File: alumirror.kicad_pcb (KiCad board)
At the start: 2 copper layers, 142.9 x 87.2 mm, 71 parts, among them J1 USB_C_Receptacle_USB2.0_16P_2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, J2 USB_C_Receptacle_USB2.0_16P_2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, K00 PG1350, K01 PG1350, K02 PG1350, K03 PG1350, K04 PG1350, K05 PG1350, K10 PG1350, K11 PG1350, K12 PG1350, K13 PG1350, K14 PG1350, K15 PG1350, K20 PG1350, K21 PG1350, K22 PG1350, K23 PG1350, K24 PG1350, K25 PG1350_1½U, K30 PG1350_1½U, K31 PG1350/SKQUCAA010, SW1 BOOT, U1 CH552T, U2 CH552T, U3 USBLC6-2P6, U4 USBLC6-2P6

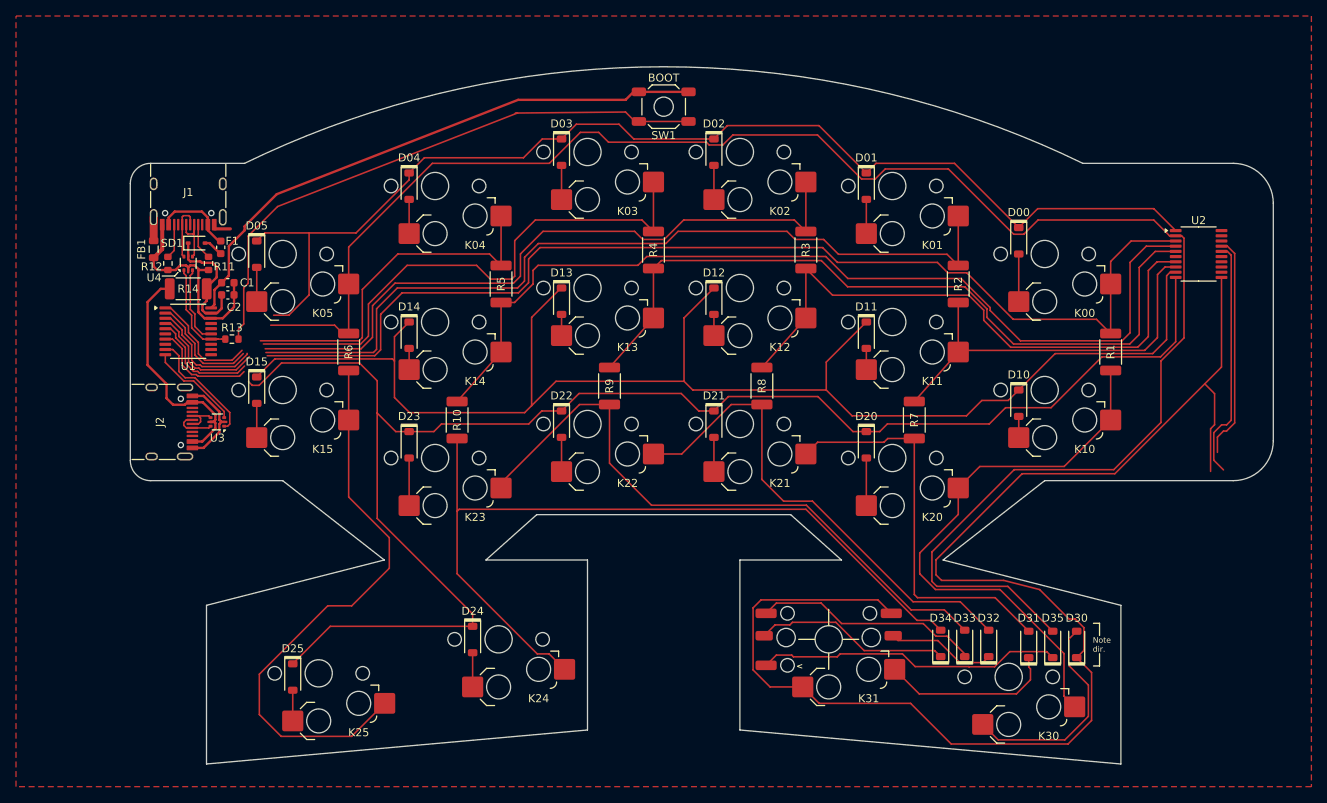
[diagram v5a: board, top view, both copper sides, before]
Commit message: Add LEDs
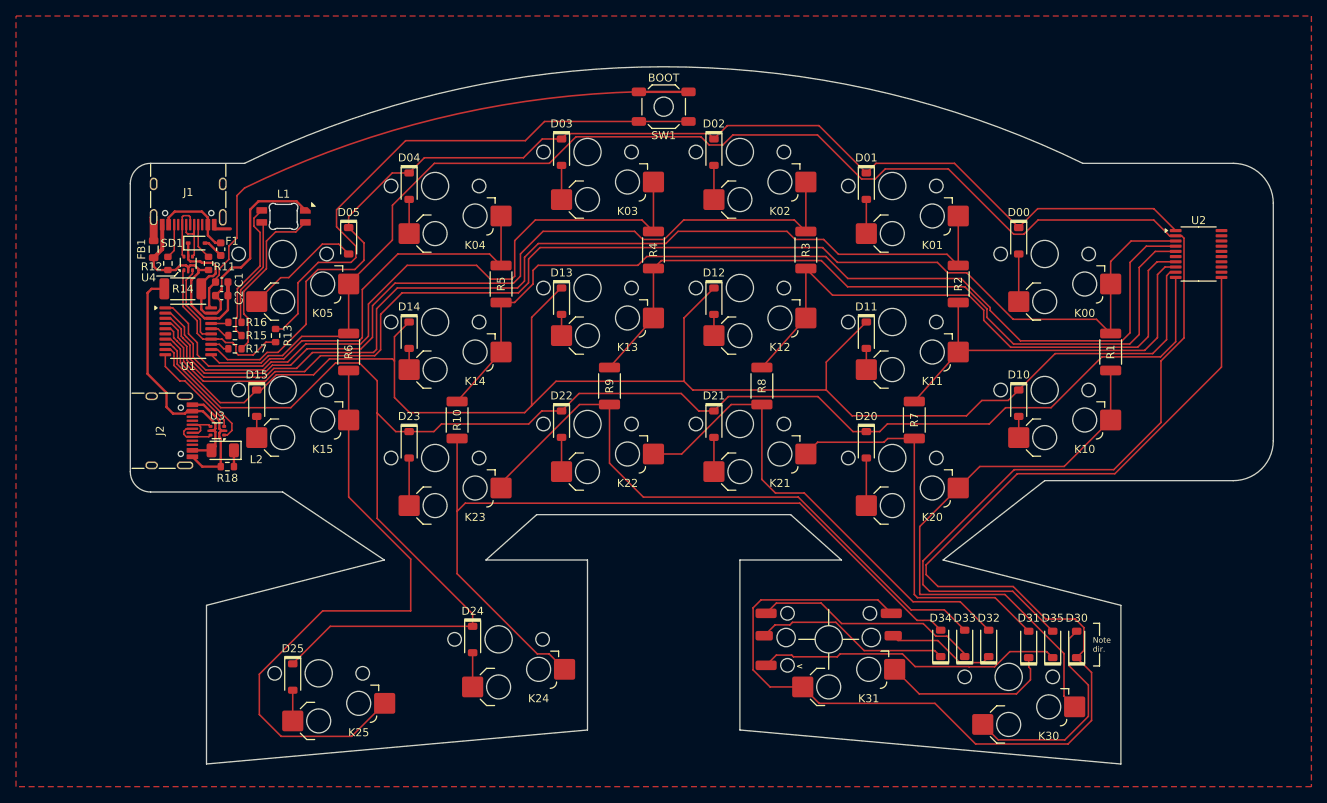
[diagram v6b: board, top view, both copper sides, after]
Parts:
- added L1: LED_6028R, PCM_marbastlib-various:LED_6028R, F.Cu at (104.9, 47.7)
- added L2: LED, LED_SMD:LED_1206_3216Metric, F.Cu at (97.3, 77.0)
- added R15: R, Resistor_SMD:R_0603_1608Metric, F.Cu at (98.8, 62.6)
- added R16: R, Resistor_SMD:R_0603_1608Metric, F.Cu at (98.8, 61.0)
- added R17: R, Resistor_SMD:R_0603_1608Metric, F.Cu at (98.8, 64.3)
- added R18: R, Resistor_SMD:R_0603_1608Metric, F.Cu at (97.9, 79.0)
- moved D05 11.6 mm to (113.0, 50.8)
- moved R13 5.48 mm to (103.9, 62.6), turned to 90 degrees
- moved D15 1.63 mm to (101.5, 71.1)
- moved J2 1.11 mm to (89.4, 74.5)
- moved U3 1.11 mm to (96.6, 74.5)
- moved C1 0.77 mm to (97.2, 55.9)
- moved C2 0.77 mm to (97.2, 57.6)
- moved R14 0.67 mm to (92.3, 56.8)
- moved F1 0.23 mm to (97.0, 51.8)
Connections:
- net +3V3_L renamed +3V3
- net BOOT_L renamed Net-(NT1-Pad1)
- net Net-(R13-Pad2) renamed /BOOT
- U1 pad 1: Col3L -> Col4L
- U1 pad 11: Col4L -> Col5
- U1 pad 12: Col5 -> Row0
- U1 pad 13: Row0 -> LED_B
- U1 pad 16: LED_B -> LED_R
- U1 pad 2: Col2L -> Col3L
- U1 pad 3: Col1L -> Col2L
- U1 pad 4: Col0 -> Col1L
- U1 pad 5: Row1 -> Col0
- U1 pad 7: Row2 -> Row1
- U1 pad 8: LED_R -> Row2
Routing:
- net +3V3: track 71.7 -> 23.1 mm
- net TX_R: track 30.0 -> 0.00 mm
- net RX_R: track 28.0 -> 0.00 mm
- net VCC_L: track 16.7 -> 38.2 mm
- net Net-(L1-BK): track 0.00 -> 21.0 mm
- net Col4L: track 44.9 -> 63.4 mm
- net Net-(L1-RK): track 0.00 -> 17.9 mm
- net Net-(L1-GK): track 0.00 -> 13.8 mm
- net Net-(D05-A): track 4.28 -> 15.0 mm
- net Col5: track 221.1 -> 231.0 mm
- net Row3R: track 177.6 -> 168.3 mm
- net Net-(NT1-Pad1): track 0.00 -> 8.67 mm
- net /Col5': track 72.1 -> 79.0 mm
- net Row0: track 144.5 -> 151.2 mm
- net Col3L: track 82.5 -> 86.5 mm
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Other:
- outline, holes or cut-outs redrawn

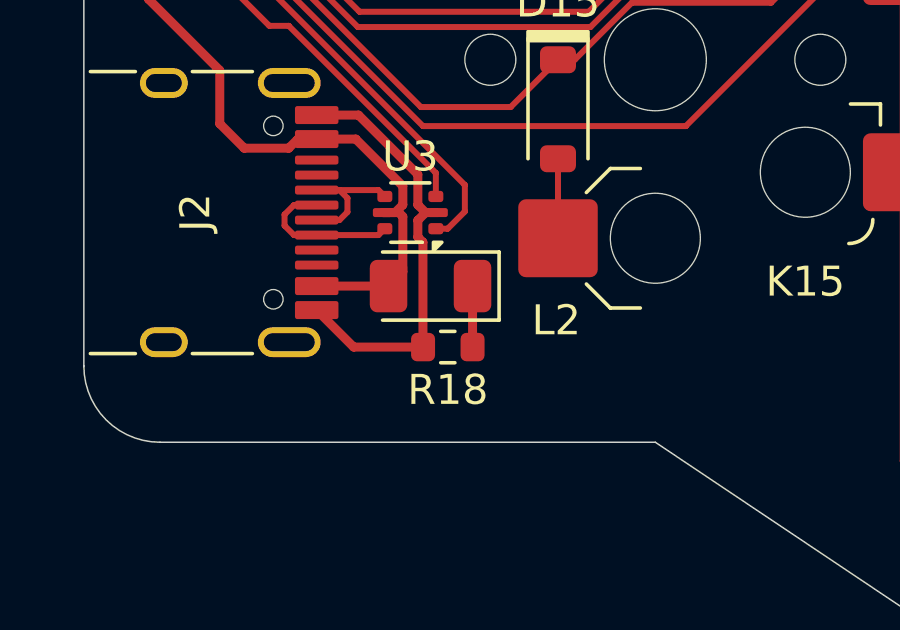
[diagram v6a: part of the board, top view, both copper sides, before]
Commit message: Use smaller (0603) power LED
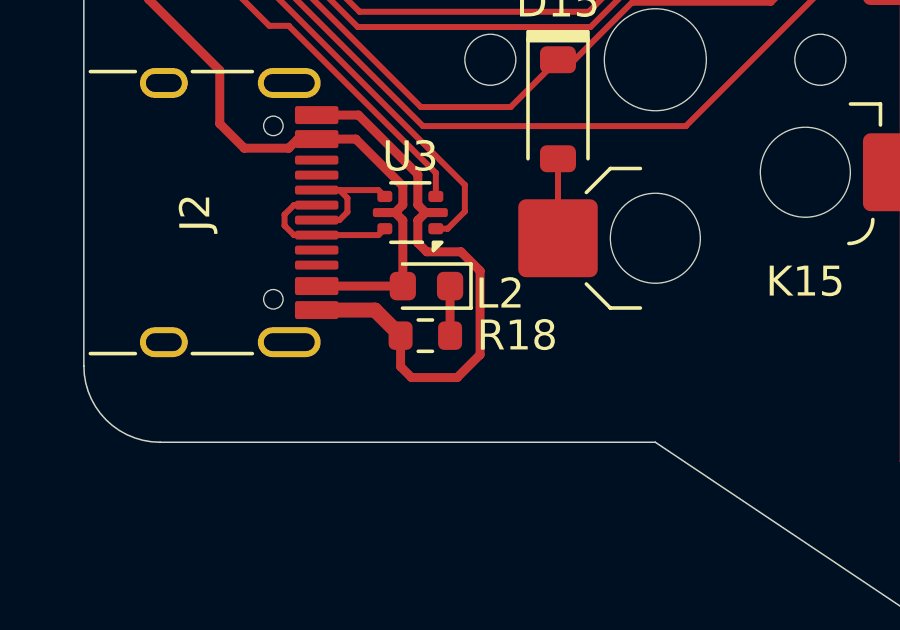
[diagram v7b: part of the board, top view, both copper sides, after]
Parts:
- L2: footprint LED_SMD:LED_1206_3216Metric -> LED_SMD:LED_0603_1608Metric
- moved R18 0.84 mm to (97.1, 78.6)
- moved L2 0.14 mm to (97.1, 77.0)
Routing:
- net GND: track 44.5 -> 49.4 mm
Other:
- board text added: "Top edge arc centre point"

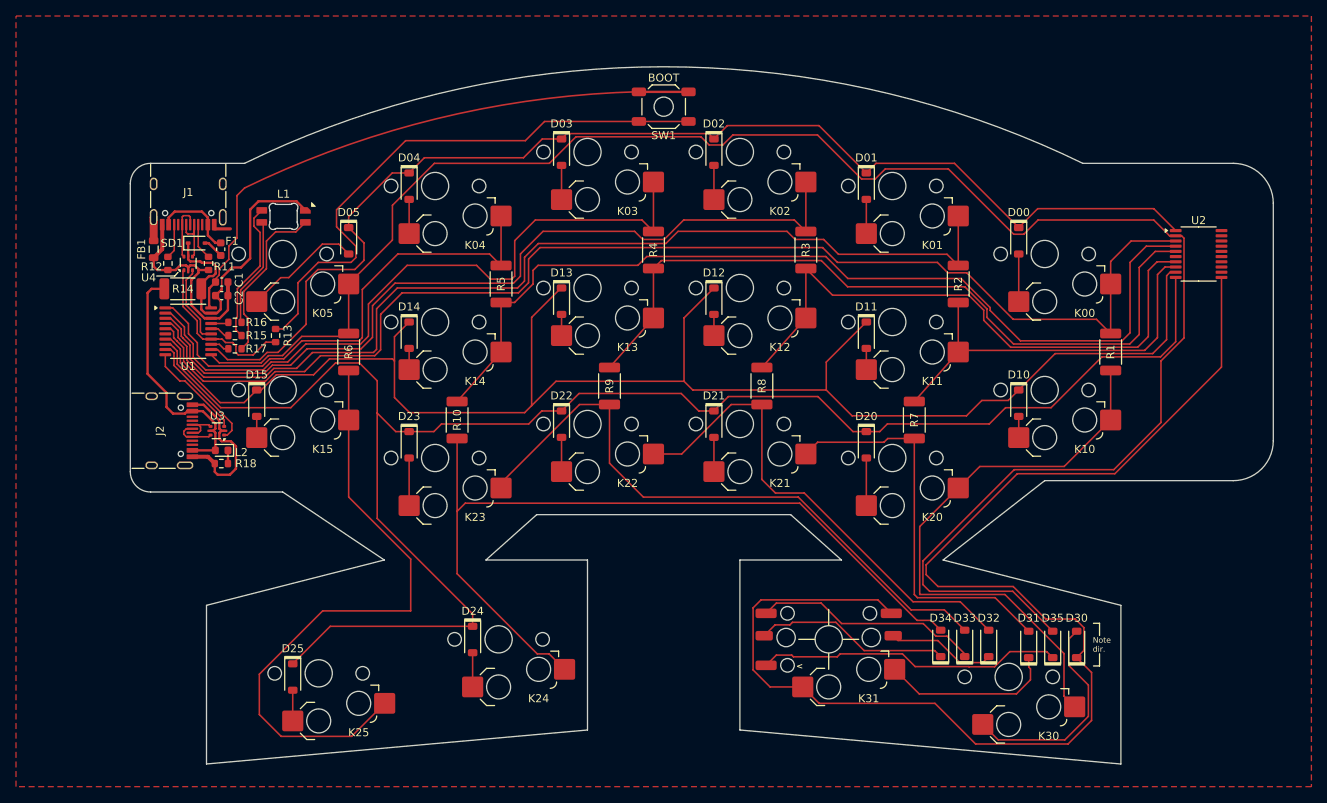
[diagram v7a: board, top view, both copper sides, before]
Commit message: Move power LED to middle of PCB above boot switch
Plus various routing tweaks and footprint updates.
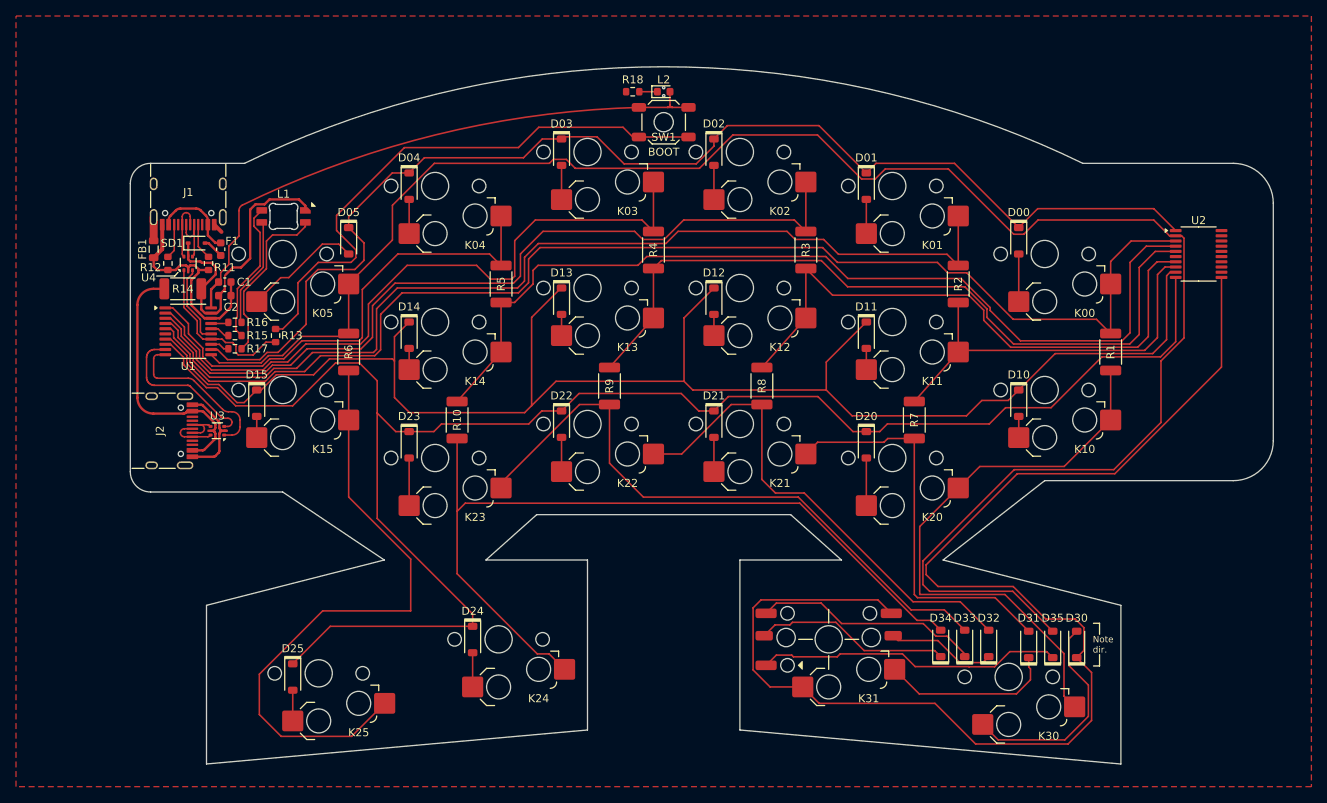
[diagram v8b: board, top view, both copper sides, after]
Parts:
- L2: footprint LED_SMD:LED_0603_1608Metric -> Project Library:LED_0603_1608Metric
- R11, R12, R13, R15, R16, R17: footprint Resistor_SMD:R_0603_1608Metric -> Project Library:R_0603_1608Metric_Mod
- R18: value R -> 10k; footprint Resistor_SMD:R_0603_1608Metric -> Project Library:R_0603_1608Metric_Mod
- moved L2 71.2 mm to (152.4, 32.1), turned to 0 degrees
- moved R18 69.3 mm to (148.5, 32.1)
- moved SW1 1.94 mm to (152.4, 35.9)
- moved C1 0.38 mm to (97.5, 55.9)
- moved C2 0.38 mm to (97.5, 57.6)
- turned NT1 to 0 degrees
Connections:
- J2 pad A6: TX_PL -> RX_PL
- J2 pad A7: RX_PL -> TX_PL
- J2 pad B6: TX_PL -> RX_PL
- J2 pad B7: RX_PL -> TX_PL
- L2 pad 2: VCC_L' -> +3V3
- NT1 pad 1: Net-(NT1-Pad1) -> USB_L+
- NT1 pad 2: USB_L+ -> Net-(NT1-Pad2)
- R13 pad 1: Net-(NT1-Pad1) -> Net-(NT1-Pad2)
- U3 pad 1: TX_L -> RX_L
- U3 pad 3: RX_L -> TX_L
- U3 pad 4: RX_PL -> TX_PL
- U3 pad 6: TX_PL -> RX_PL
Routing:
- net Net-(NT1-Pad2): track 0.00 -> 8.67 mm
- net Net-(NT1-Pad1): track 8.67 -> 0.00 mm
- net RX_L: track 12.4 -> 20.3 mm
- net GND: track 49.4 -> 41.7 mm
- net TX_L: track 15.2 -> 19.8 mm
- net Row0: track 151.2 -> 153.6 mm
- net +3V3: track 23.1 -> 20.9 mm
- net VCC_L': track 31.6 -> 33.5 mm
- net /BOOT: track 71.5 -> 70.6 mm
- net VBUS_L: track 10.6 -> 9.68 mm
- net Col4L: track 63.4 -> 62.5 mm
- net RX_PL: track 5.10 -> 5.88 mm
- net TX_PL: track 5.13 -> 5.88 mm
- net Row2: track 212.9 -> 212.3 mm
- net Net-(L2-K): track 1.65 -> 2.26 mm
